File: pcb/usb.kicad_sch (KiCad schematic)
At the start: 4 parts, among them J22 USB_C_Receptacle_USB2.0_16P, U20 SMF05CT1G-ES

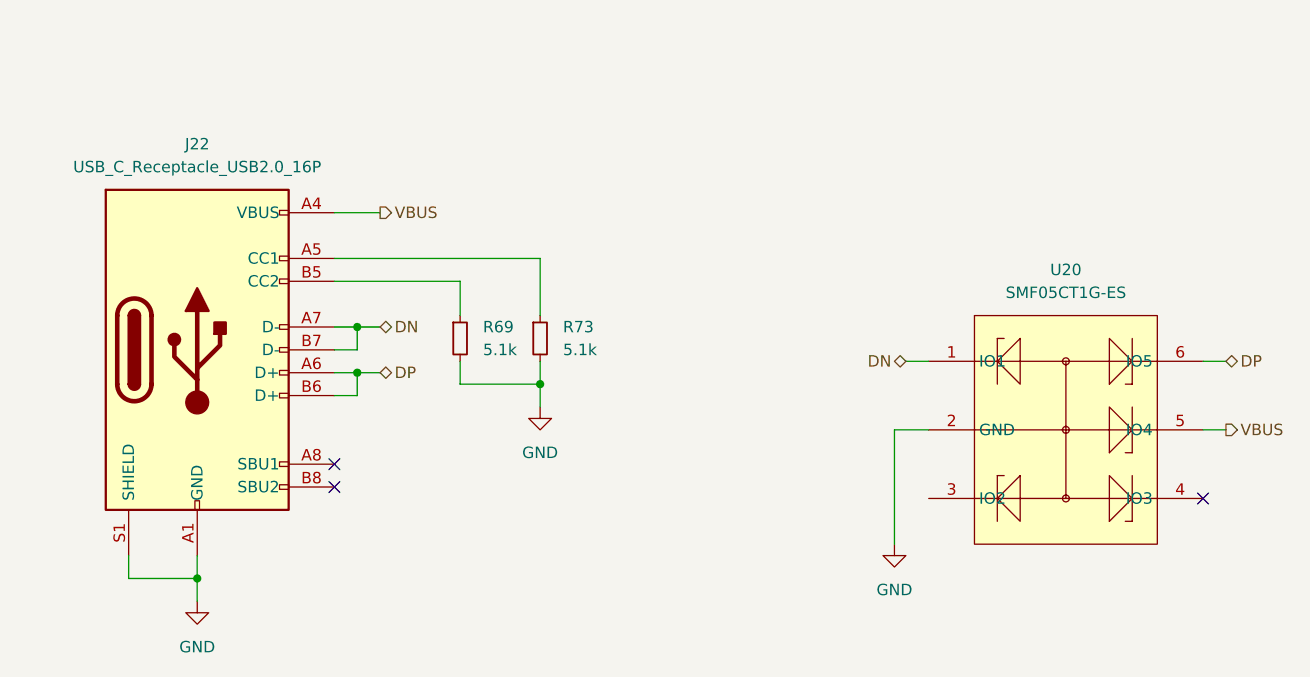
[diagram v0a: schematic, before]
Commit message: change usb-c to tht type
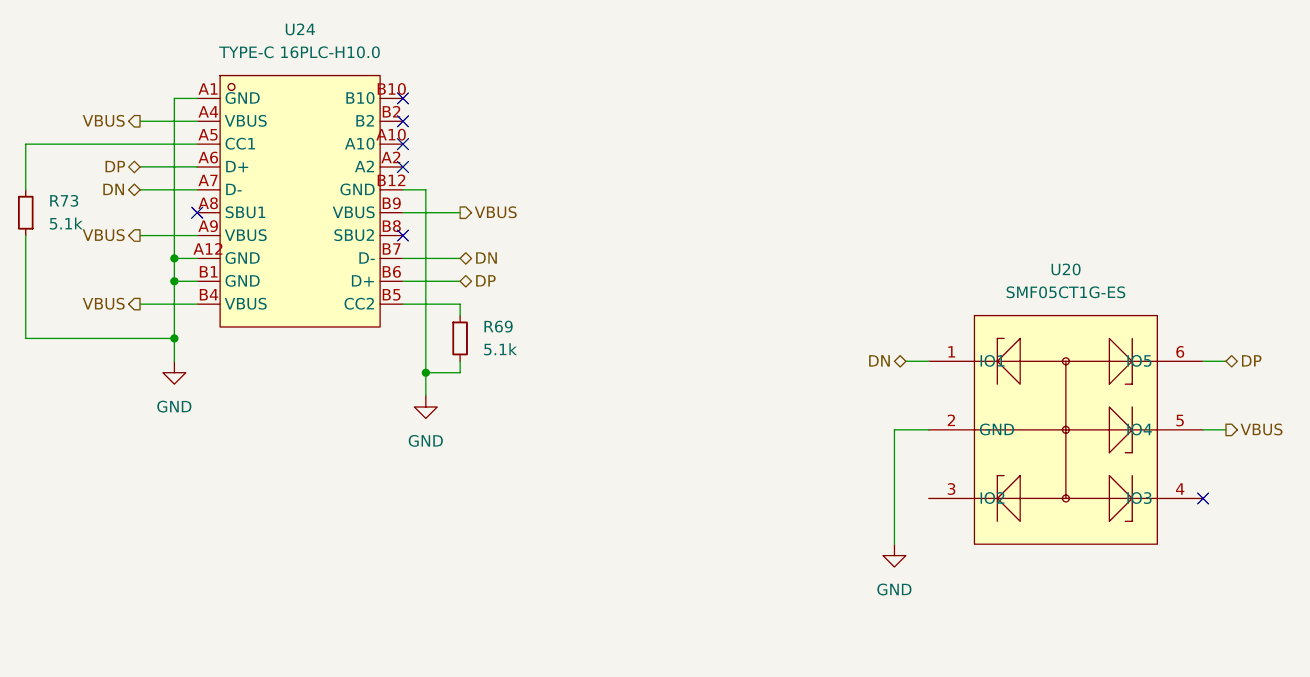
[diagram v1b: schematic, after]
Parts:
- removed J22: USB_C_Receptacle_USB2.0_16P, Connector_USB:USB_C_Receptacle_G-Switch_GT-USB-7051x, symbol Connector:USB_C_Receptacle_USB2.0_16P
- added U24: TYPE-C 16PLC-H10.0, Longboi_Custom:TYPE-C-TH_16PLC-H10.0, symbol Longboi_Custom:TYPE-C16PLC-H10.0
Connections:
- net DN: now also U24.A7 (D-), U24.B7 (D-)
- net DP: now also U24.A6 (D+), U24.B6 (D+)
- net GND: now also R73.1, U24.A1 (GND), U24.A12 (GND), U24.B1 (GND), U24.B12 (GND); no longer R73.2
- net VBUS: now also U24.A4 (VBUS), U24.A9 (VBUS), U24.B4 (VBUS), U24.B9 (VBUS)
- net at R69.1: now also U24.B5 (CC2)
- new net: R73.2, U24.A5 (CC1)
- no-connect marks 3 -> 7
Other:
- moved on the sheet: R73

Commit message: fixes #18 fixes #26
replace usb-c connector
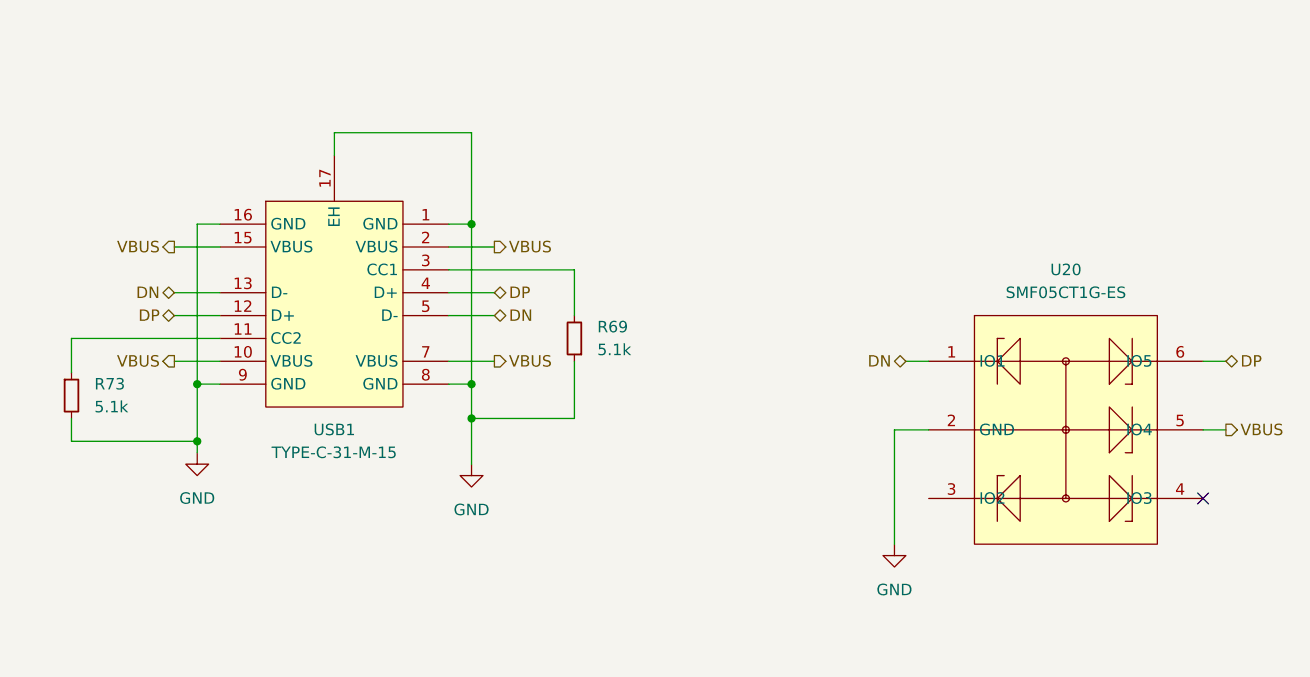
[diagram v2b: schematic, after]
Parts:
- removed U24: TYPE-C 16PLC-H10.0, Longboi_Custom:TYPE-C-TH_16PLC-H10.0, symbol Longboi_Custom:TYPE-C16PLC-H10.0
- added USB1: TYPE-C-31-M-15, Longboi_Custom:USBC-TH_TYPE-C-31-M-15, symbol Longboi_Custom:TYPE-C-31-M-15
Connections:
- net DN: now also USB1.13 (D-), USB1.5 (D-)
- net DP: now also USB1.12 (D+), USB1.4 (D+)
- net GND: now also R69.1, R73.2, USB1.1 (GND), USB1.16 (GND), USB1.17 (EH), USB1.8 (GND), USB1.9 (GND); no longer R69.2, R73.1
- net VBUS: now also USB1.10 (VBUS), USB1.15 (VBUS), USB1.2 (VBUS), USB1.7 (VBUS)
- new net: R69.2, USB1.3 (CC1)
- new net: R73.1, USB1.11 (CC2)
- no-connect marks 7 -> 1
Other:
- moved on the sheet: R69, R73
